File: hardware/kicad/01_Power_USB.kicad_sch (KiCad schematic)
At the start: 12 parts, among them J1 TYPE-C-31-M-12, U1 TPD2EUSB30DRTR, U2 TLV62569DBVR

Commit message: Resolve KiCad component sourcing and missing footprints
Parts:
- L1: value 2.2uH - Isat TBD -> 2.2uH; footprint (none) -> Inductor_SMD:L_Sunlord_SWPA4020S; Checked (none) -> 2026-09-08; JLCPCB Library Type (none) -> Extended; JLCPCB Part # (none) -> C83423; LCSC (none) -> C83423; MPN (none) -> SWPA4020S2R2MT; Manufacturer (none) -> Sunlord; Sourcing Status TBD - select shielded power inductor and verified footprint -> JLCPCB catalog verified; stock/quote refresh required; Supplier URL (none) -> https://jlcpcb.com/partdetail/Sunlord-SWPA4020S2R2MT/C83423
- R1: Checked (none) -> 2026-09-08; JLCPCB Library Type (none) -> Basic; JLCPCB Part # (none) -> C25803; LCSC (none) -> C25803; MPN (none) -> 0603WAF1003T5E; Manufacturer (none) -> UNI-ROYAL; Sourcing Status TBD - not orderable -> JLCPCB catalog verified; stock/quote refresh required; Supplier URL (none) -> https://jlcpcb.com/partdetail/C25803
- R2: Checked (none) -> 2026-09-08; JLCPCB Library Type (none) -> Extended; JLCPCB Part # (none) -> C25961; LCSC (none) -> C25961; MPN (none) -> 0603WAF2212T5E; Manufacturer (none) -> UNI-ROYAL; Sourcing Status TBD - not orderable -> JLCPCB catalog verified; stock/quote refresh required; Supplier URL (none) -> https://jlcpcb.com/partdetail/26704-0603WAF2212T5E/C25961
- U1: Checked (none) -> 2026-09-08; JLCPCB Library Type (none) -> Extended; JLCPCB Part # (none) -> C97502; LCSC (none) -> C97502; Sourcing Status TBD - not orderable -> JLCPCB catalog verified; stock/quote refresh required; Supplier URL (none) -> https://jlcpcb.com/partdetail/TexasInstruments-TPD2EUSB30DR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
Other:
- note added: "DRAFT 0.2 - CIRCUIT DEVELOPMENT ONLY - NOT FOR FABRICATION"
- note added: "Nominal output: 0.6 V x (1 + 100k / 22.1k) = 3.315 V. SWPA4020S2R2MT / 20 uF filter; verify bias, stability and thermals. Provisional logic-rail target: <=1 A continuous pending thermal tests. PWR_5V_PENDING and ACT_5V_PENDING have no source in this draft."
- note removed: "DRAFT 0.1 - CIRCUIT DEVELOPMENT ONLY - NOT FOR FABRICATION"
- note removed: "Nominal output: 0.6 V x (1 + 100k / 22.1k) = 3.315 V. 2.2 uH / 20 uF is a starting filter; verify bias, stability and thermals. Divider tolerance and full-load regulation still require review. PWR_5V_PENDING and ACT_5V_PENDING have no source in this draft."
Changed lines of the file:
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@@
     (title "MagMouse - 01_Power_USB")
     (date "2026-09-08")
-    (rev "0.1 DRAFT")
+    (rev "0.2 DRAFT")
     (company "MagMouse")
     (comment 1 "NOT FOR FABRICATION - unresolved circuits listed in README.md"))
@@
       (justify left top))
 )
-  (text "DRAFT 0.1 - CIRCUIT DEVELOPMENT ONLY - NOT FOR FABRICATION"
+  (text "DRAFT 0.2 - CIRCUIT DEVELOPMENT ONLY - NOT FOR FABRICATION"
     (at 20 24 0)
     (effects
@@
           (size 1.0 1.0))
         (justify left)))
-    (property "LCSC" ""
+    (property "LCSC" "C97502"
       (at 137.16 73.66 0)
       (hide yes)
@@
           (size 1.0 1.0))
         (justify left)))
-    (property "JLCPCB Part #" ""
+    (property "JLCPCB Part #" "C97502"
       (at 137.16 73.66 0)
       (hide yes)
@@
           (size 1.0 1.0))
         (justify left)))
-    (property "Sourcing Status" "TBD - not orderable"
+    (property "Sourcing Status" "JLCPCB catalog verified; stock/quote refresh required"
       (at 137.16 73.66 0)
       (hide yes)
@@
           (size 1.0 1.0))
         (justify left)))
-    (property "Checked" ""
+    (property "Checked" "2026-09-08"
       (at 137.16 73.66 0)
       (hide yes)
@@
         (path "/5d73110b-42e6-5c5c-9841-c82d60f67640/f98db9d6-39f0-56d0-b006-a308a0af27b1"
           (reference "U1")
-          (unit 1)))))
+          (unit 1))))
+    (property "Supplier URL" "https://jlcpcb.com/partdetail/TexasInstruments-TPD2EUSB30DRTR/C97502"
+      (at 137.16 73.66 0)
+      (hide yes)
+      (effects
+        (font
+          (size 1 1))
+        (justify left)))
+    (property "JLCPCB Library Type" "Extended"
+      (at 137.16 73.66 0)
+      (hide yes)
+      (effects
+        (font
+          (size 1 1))
+        (justify left))))
   (wire
     (pts
@@
           (size 1.0 1.0))
         (justify left)))
-    (property "Value" "2.2uH - Isat TBD"
+    (property "Value" "2.2uH"
       (at 291.02 54.34 0)
       (effects
@@
           (size 1.0 1.0))
         (justify left)))
-    (property "Footprint" ""
+    (property "Footprint" "Inductor_SMD:L_Sunlord_SWPA4020S"
       (at 287.02 53.34 0)
       (hide yes)
@@
           (size 1.0 1.0))
         (justify left)))
-    (property "Datasheet" ""
+    (property "Datasheet" "https://atta.szlcsc.com/upload/public/pdf/source/20210916/AC798BA7E846B7D0B6818F45CD84DB0B.pdf"
       (at 287.02 53.34 0)
       (hide yes)
@@
           (size 1.0 1.0))
         (justify left)))
-    (property "Manufacturer" ""
+    (property "Manufacturer" "Sunlord"
       (at 287.02 53.34 0)
       (hide yes)
@@
           (size 1.0 1.0))
         (justify left)))
-    (property "MPN" ""
+    (property "MPN" "SWPA4020S2R2MT"
       (at 287.02 53.34 0)
       (hide yes)
@@
           (size 1.0 1.0))
         (justify left)))
-    (property "LCSC" ""
+    (property "LCSC" "C83423"
       (at 287.02 53.34 0)
       (hide yes)
@@
           (size 1.0 1.0))
         (justify left)))
-    (property "JLCPCB Part #" ""
+    (property "JLCPCB Part #" "C83423"
       (at 287.02 53.34 0)
       (hide yes)
@@
           (size 1.0 1.0))
         (justify left)))
-    (property "Sourcing Status" "TBD - select shielded power inductor and verified footprint"
+    (property "Sourcing Status" "JLCPCB catalog verified; stock/quote refresh required"
       (at 287.02 53.34 0)
       (hide yes)
@@
           (size 1.0 1.0))
         (justify left)))
-    (property "Checked" ""
+    (property "Checked" "2026-09-08"
       (at 287.02 53.34 0)
       (hide yes)
@@
         (path "/5d73110b-42e6-5c5c-9841-c82d60f67640/f98db9d6-39f0-56d0-b006-a308a0af27b1"
           (reference "L1")
-          (unit 1)))))
+          (unit 1))))
+    (property "Supplier URL" "https://jlcpcb.com/partdetail/Sunlord-SWPA4020S2R2MT/C83423"
+      (at 287.02 53.34 0)
+      (hide yes)
+      (effects
+        (font
+          (size 1 1))
+        (justify left)))
+    (property "JLCPCB Library Type" "Extended"
+      (at 287.02 53.34 0)
+      (hide yes)
+      (effects
+        (font
+          (size 1 1))
+        (justify left))))
   (wire
     (pts
@@
           (size 1.0 1.0))
         (justify left)))
-    (property "Manufacturer" ""
+    (property "Manufacturer" "UNI-ROYAL"
       (at 274.32 101.6 0)
       (hide yes)
@@
           (size 1.0 1.0))
         (justify left)))
-    (property "MPN" ""
+    (property "MPN" "0603WAF1003T5E"
       (at 274.32 101.6 0)
       (hide yes)
@@
           (size 1.0 1.0))
         (justify left)))
-    (property "LCSC" ""
+    (property "LCSC" "C25803"
       (at 274.32 101.6 0)
       (hide yes)
@@
           (size 1.0 1.0))
         (justify left)))
-    (property "JLCPCB Part #" ""
+    (property "JLCPCB Part #" "C25803"
       (at 274.32 101.6 0)
       (hide yes)
@@
           (size 1.0 1.0))
         (justify left)))
-    (property "Sourcing Status" "TBD - not orderable"
+    (property "Sourcing Status" "JLCPCB catalog verified; stock/quote refresh required"
       (at 274.32 101.6 0)
       (hide yes)
@@
           (size 1.0 1.0))
         (justify left)))
-    (property "Checked" ""
+    (property "Checked" "2026-09-08"
       (at 274.32 101.6 0)
       (hide yes)
@@
         (path "/5d73110b-42e6-5c5c-9841-c82d60f67640/f98db9d6-39f0-56d0-b006-a308a0af27b1"
           (reference "R1")
-          (unit 1)))))
+          (unit 1))))
+    (property "Supplier URL" "https://jlcpcb.com/partdetail/C25803"
+      (at 274.32 101.6 0)
+      (hide yes)
+      (effects
+        (font
+          (size 1 1))
+        (justify left)))
+    (property "JLCPCB Library Type" "Basic"
+      (at 274.32 101.6 0)
+      (hide yes)
+      (effects
+        (font
+          (size 1 1))
+        (justify left))))
   (wire
     (pts
@@
           (size 1.0 1.0))
         (justify left)))
-    (property "Manufacturer" ""
+    (property "Manufacturer" "UNI-ROYAL"
       (at 274.32 134.62 0)
       (hide yes)
@@
           (size 1.0 1.0))
         (justify left)))
-    (property "MPN" ""
+    (property "MPN" "0603WAF2212T5E"
       (at 274.32 134.62 0)
       (hide yes)
@@
           (size 1.0 1.0))
         (justify left)))
-    (property "LCSC" ""
+    (property "LCSC" "C25961"
       (at 274.32 134.62 0)
       (hide yes)
@@
           (size 1.0 1.0))
         (justify left)))
-    (property "JLCPCB Part #" ""
+    (property "JLCPCB Part #" "C25961"
       (at 274.32 134.62 0)
       (hide yes)
@@
           (size 1.0 1.0))
         (justify left)))
-    (property "Sourcing Status" "TBD - not orderable"
+    (property "Sourcing Status" "JLCPCB catalog verified; stock/quote refresh required"
       (at 274.32 134.62 0)
       (hide yes)
@@
           (size 1.0 1.0))
         (justify left)))
-    (property "Checked" ""
+    (property "Checked" "2026-09-08"
       (at 274.32 134.62 0)
       (hide yes)
@@
         (path "/5d73110b-42e6-5c5c-9841-c82d60f67640/f98db9d6-39f0-56d0-b006-a308a0af27b1"
           (reference "R2")
-          (unit 1)))))
+          (unit 1))))
+    (property "Supplier URL" "https://jlcpcb.com/partdetail/26704-0603WAF2212T5E/C25961"
+      (at 274.32 134.62 0)
+      (hide yes)
+      (effects
+        (font
+          (size 1 1))
+        (justify left)))
+    (property "JLCPCB Library Type" "Extended"
+      (at 274.32 134.62 0)
+      (hide yes)
+      (effects
+        (font
+          (size 1 1))
+        (justify left))))
   (wire
     (pts
@@
     (color 0 0 0 0)
 )
-  (text "Nominal output: 0.6 V x (1 + 100k / 22.1k) = 3.315 V.\n2.2 uH / 20 uF is a starting filter; verify bias, stability and thermals.\nDivider tolerance and full-load regulation still require review.\nPWR_5V_PENDING and ACT_5V_PENDING have no source in this draft."
+  (text "Nominal output: 0.6 V x (1 + 100k / 22.1k) = 3.315 V.\nSWPA4020S2R2MT / 20 uF filter; verify bias, stability and thermals.\nProvisional logic-rail target: <=1 A continuous pending thermal tests.\nPWR_5V_PENDING and ACT_5V_PENDING have no source in this draft."
     (at 190 163 0)
     (effects

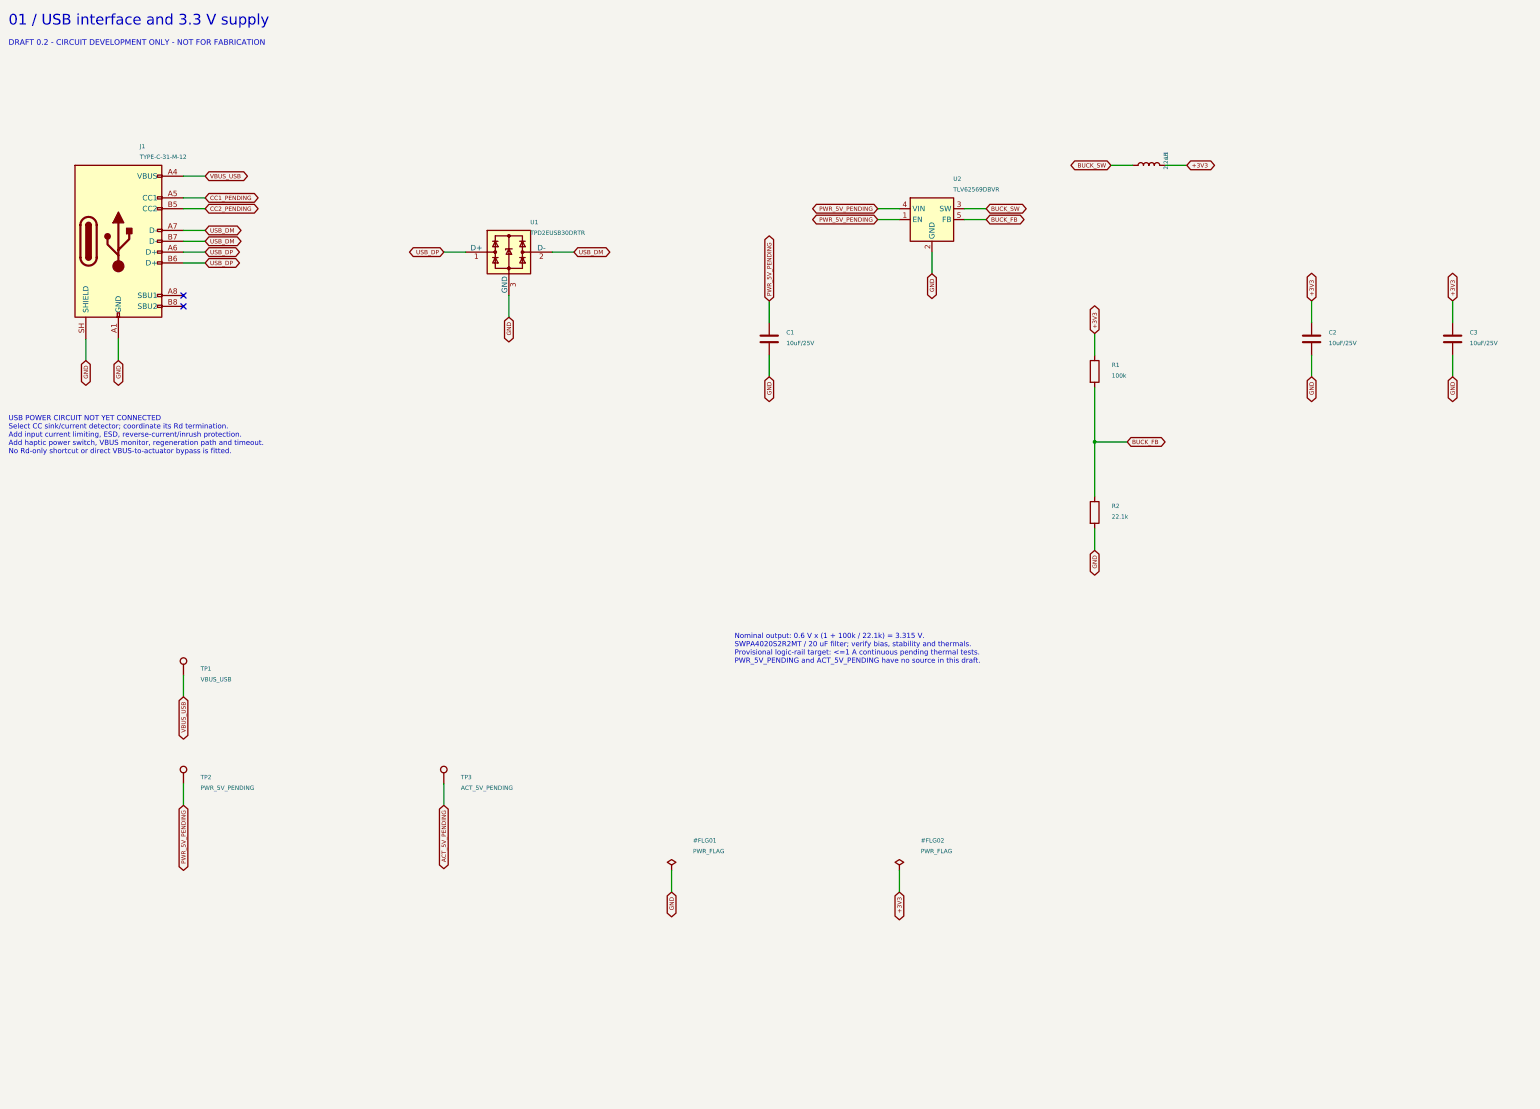
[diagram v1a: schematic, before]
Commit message: Implement USB-C power control schematic and validation
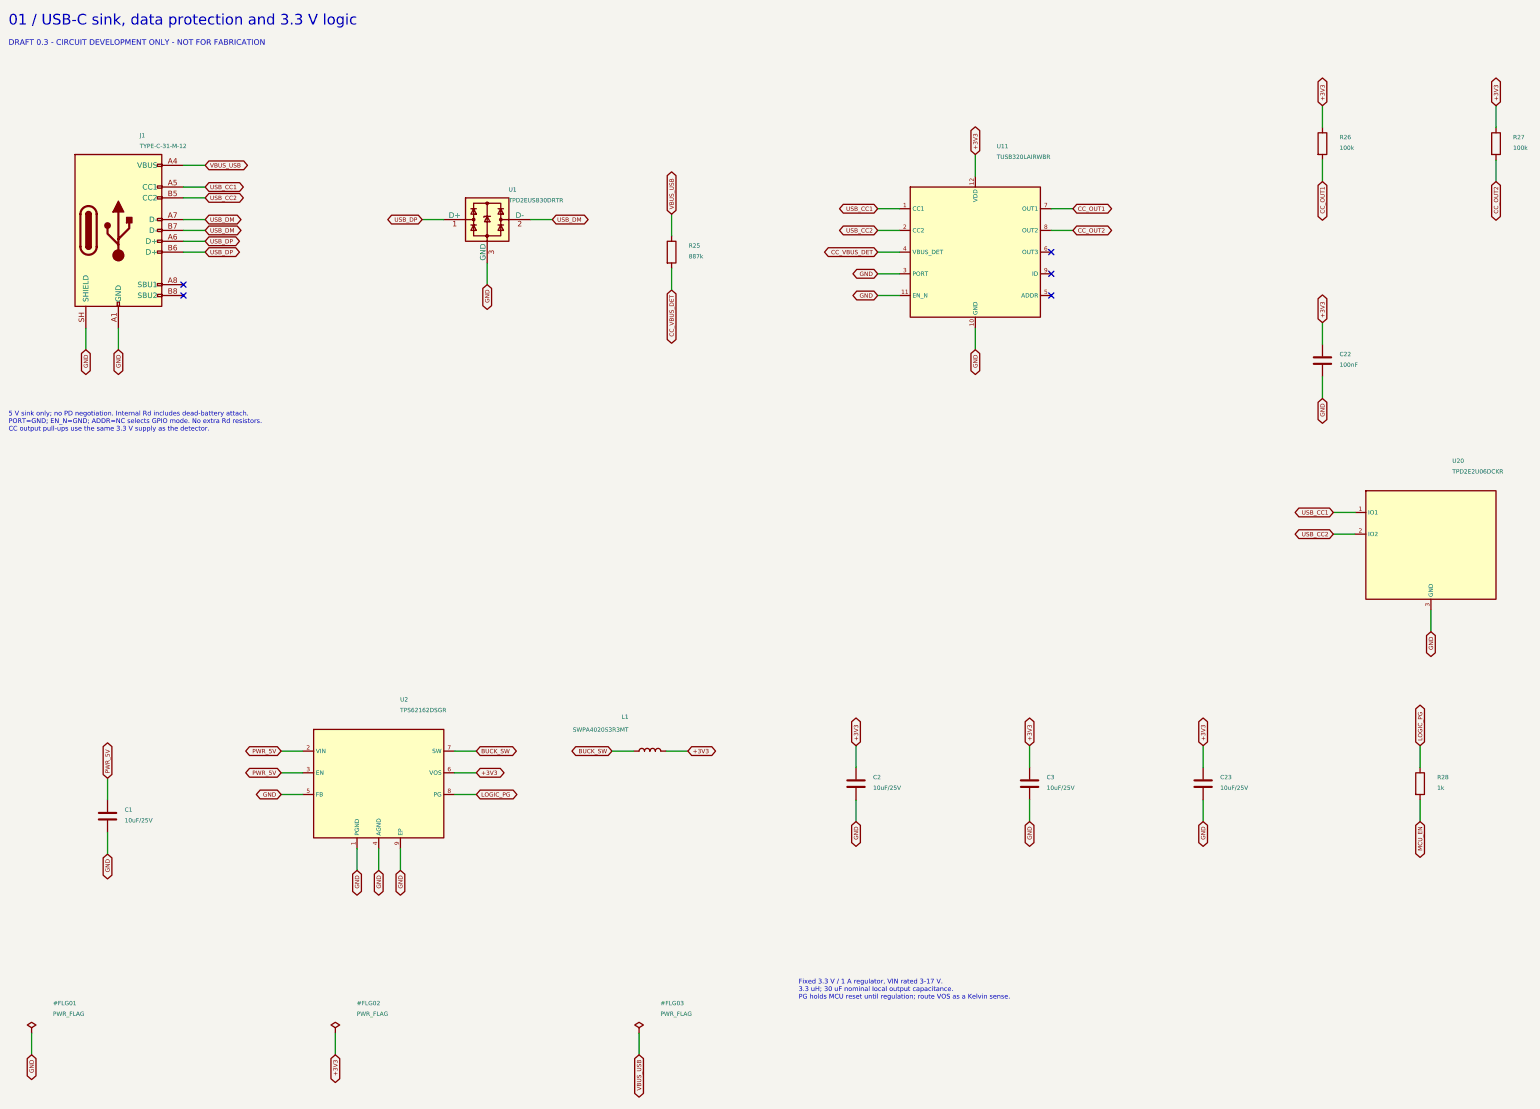
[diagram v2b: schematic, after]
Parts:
- removed R1: 100k, Resistor_SMD:R_0603_1608Metric, symbol Device:R
- removed R2: 22.1k, Resistor_SMD:R_0603_1608Metric, symbol Device:R
- removed TP1: VBUS_USB, TestPoint:TestPoint_Pad_D1.0mm, symbol Connector:TestPoint
- removed TP2: PWR_5V_PENDING, TestPoint:TestPoint_Pad_D1.0mm, symbol Connector:TestPoint
- removed TP3: ACT_5V_PENDING, TestPoint:TestPoint_Pad_D1.0mm, symbol Connector:TestPoint
- added C22: 100nF, Capacitor_SMD:C_0603_1608Metric, symbol Device:C
- added C23: 10uF/25V, Capacitor_SMD:C_0805_2012Metric, symbol Device:C
- added R25: 887k, Resistor_SMD:R_0603_1608Metric, symbol Device:R
- added R26, R27: 100k, Resistor_SMD:R_0603_1608Metric, symbol Device:R
- added R28: 1k, Resistor_SMD:R_0603_1608Metric, symbol Device:R
- added U11: TUSB320LAIRWBR, Package_DFN_QFN:Texas_X2QFN-12_1.6x1.6mm_P0.4mm, symbol MagMouse:TUSB320LAIRWBR
- added U20: TPD2E2U06DCKR, Package_TO_SOT_SMD:SOT-323_SC-70, symbol MagMouse:TPD2E2U06DCKR
- L1: value 2.2uH -> SWPA4020S3R3MT; JLCPCB Library Type Extended -> (none); JLCPCB Part # C83423 -> C83424; LCSC C83423 -> C83424; MPN SWPA4020S2R2MT -> SWPA4020S3R3MT; Sourcing Status JLCPCB catalog verified; stock/quote refresh required -> Catalog MPN verified 2026-09-08; stock and assembly quote m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; Supplier URL https://jlcpcb.com/partdetail/Sunlord-SWPA4020S2R2MT/C83423 -> https://www.lcsc.com/product-detail/C83424.html
- U1: JLCPCB Library Type Extended -> (none)
- U2: value TLV62569DBVR -> TPS62162DSGR; footprint Package_TO_SOT_SMD:SOT-23-5 -> Package_SON:Texas_DSG0008A_WSON-8-1EP_2x2mm_P0.5mm_EP0.9x1.6mm; symbol Regulator_Switching:TLV62569DBV -> MagMouse:TPS62162DSGR; JLCPCB Part # C141836 -> C40256; LCSC C141836 -> C40256; MPN TLV62569DBVR -> TPS62162DSGR; Sourcing Status JLCPCB listing verified; stock/quote pending -> Catalog MPN verified 2026-09-08; stock and assembly quote m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; Supplier URL https://www.lcsc.com/product-detail/C141836.html -> https://www.lcsc.com/product-detail/C40256.html
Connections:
- net BUCK_FB is gone; now on net GND: U2.5 (FB)
- net +3V3: now also U2.6 (VOS), C22.1, C23.1, R26.1, R27.1, U11.12 (VDD)
- net BUCK_SW: now also U2.7 (SW); no longer U2.3 (SW)
- net GND: now also U2.1 (PGND), U2.4 (AGND), U2.9 (EP), C22.2, C23.2, U11.10 (GND), U11.11 (EN_N), U11.3 (PORT), U20.3 (GND); no longer U2.2 (GND)
- net VBUS_USB: now also R25.1
- net CC1_PENDING renamed USB_CC1
- net USB_CC1: now also U11.1 (CC1), U20.1 (IO1)
- net CC2_PENDING renamed USB_CC2
- net USB_CC2: now also U11.2 (CC2), U20.2 (IO2)
- removed net PWR_5V_PENDING: C1.1, U2.1 (EN), U2.4 (VIN)
- new net CC_OUT1: R26.2, U11.7 (OUT1)
- new net CC_OUT2: R27.2, U11.8 (OUT2)
- new net CC_VBUS_DET: R25.2, U11.4 (VBUS_DET)
- new net LOGIC_PG: R28.1, U2.8 (PG)
- new net MCU_EN: R28.2
- new net PWR_5V: C1.1, U2.2 (VIN), U2.3 (EN)
- no-connect marks 2 -> 5
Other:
- note added: "01 / USB-C sink, data protection and 3.3 V logic"
- note added: "5 V sink only; no PD negotiation. Internal Rd includes dead-battery attach. PORT=GND; EN_N=GND; ADDR=NC selects GPIO mode. No extra Rd resistors. CC output pull-ups use the same 3.3 V supply as the detector."
- note added: "DRAFT 0.3 - CIRCUIT DEVELOPMENT ONLY - NOT FOR FABRICATION"
- note added: "Fixed 3.3 V / 1 A regulator, VIN rated 3-17 V. 3.3 uH; 30 uF nominal local output capacitance. PG holds MCU reset until regulation; route VOS as a Kelvin sense."
- note removed: "01 / USB interface and 3.3 V supply"
- note removed: "DRAFT 0.2 - CIRCUIT DEVELOPMENT ONLY - NOT FOR FABRICATION"
- note removed: "Nominal output: 0.6 V x (1 + 100k / 22.1k) = 3.315 V. SWPA4020S2R2MT / 20 uF filter; verify bias, stability and thermals. Provisional logic-rail target: <=1 A continuous pending thermal tests. PWR_5V_PENDING and ACT_5V_PENDING have no source in this draft."
- note removed: "USB POWER CIRCUIT NOT YET CONNECTED Select CC sink/current detector; coordinate its Rd termination. Add input current limiting, ESD, reverse-current/inrush protection. Add haptic power switch, VBUS monitor, regeneration path and timeout. No Rd-only shortcut or direct VBUS-to-actuator bypass is fitted."
- moved on the sheet: C1, C2, C3, J1, L1, U1

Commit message: Allocate ESP32-S3 GPIO and peripheral resources
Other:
- note added: "DRAFT 0.4 - CIRCUIT DEVELOPMENT ONLY - NOT FOR FABRICATION"
- note removed: "DRAFT 0.3 - CIRCUIT DEVELOPMENT ONLY - NOT FOR FABRICATION"
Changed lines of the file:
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@@
     (title "MagMouse - 01_Power_USB")
     (date "2026-09-08")
-    (rev "0.3 DRAFT")
+    (rev "0.4 DRAFT")
     (company "MagMouse")
     (comment 1 "NOT FOR FABRICATION - unresolved circuits listed in README.md"))
@@
       (justify left top))
 )
-  (text "DRAFT 0.3 - CIRCUIT DEVELOPMENT ONLY - NOT FOR FABRICATION"
+  (text "DRAFT 0.4 - CIRCUIT DEVELOPMENT ONLY - NOT FOR FABRICATION"
     (at 20 24 0)
     (effects
